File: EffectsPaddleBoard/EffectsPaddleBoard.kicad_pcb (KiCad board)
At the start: 4 copper layers, 89.6 x 66.6 mm, 90 parts, among them J1 Conn_01x03_Pin, J2 Conn_01x06_Pin, J3 Barrel_Jack, J4 Conn_01x04_Pin, J5 AudioJack2, J6 AudioJack2, SW1 SW_SPDT, SW2 SW_Push, SW3 SW_SPDT, U1 STM32F405RGTx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

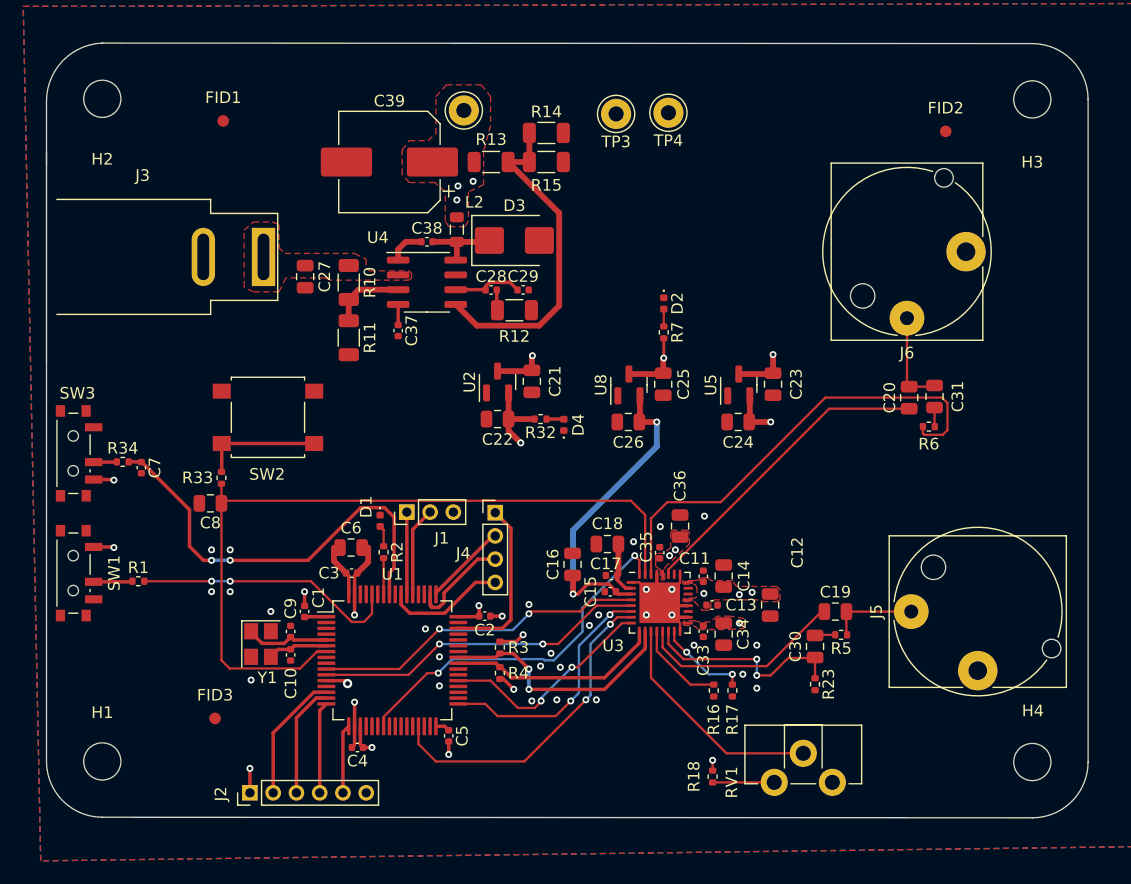
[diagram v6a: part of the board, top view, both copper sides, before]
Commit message: Eliminated all except 2 DRC errors
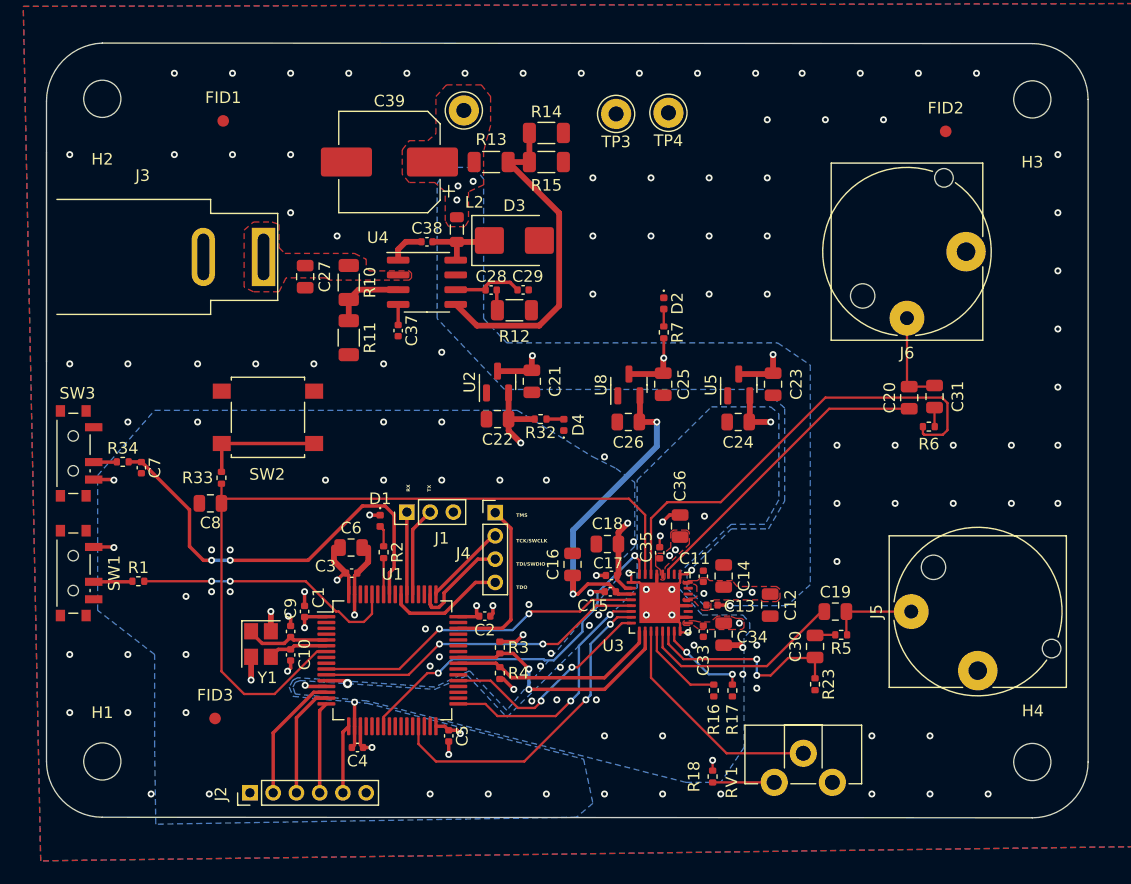
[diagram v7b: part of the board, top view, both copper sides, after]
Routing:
- net GND: track 33.2 -> 50.1 mm, vias 35 -> 136
- net +3.3V: track 34.1 -> 37.3 mm, vias 8 -> 11
- net Codec_Reset: track 67.3 -> 69.8 mm
- net +3.3VA: track 5.01 -> 6.88 mm, vias 5 -> 6
- added copper zone on B.Cu, net +3.3V
- added copper zone on B.Cu, net +3.3VA
- added copper zone on B.Cu, net +5V
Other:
- outline, holes or cut-outs redrawn
- board text added: "RX"
- board text added: "TCK/SWCLK"
- board text added: "TDI/SWDIO"
- board text added: "TDO"
- board text added: "TMS"
- board text added: "TX"

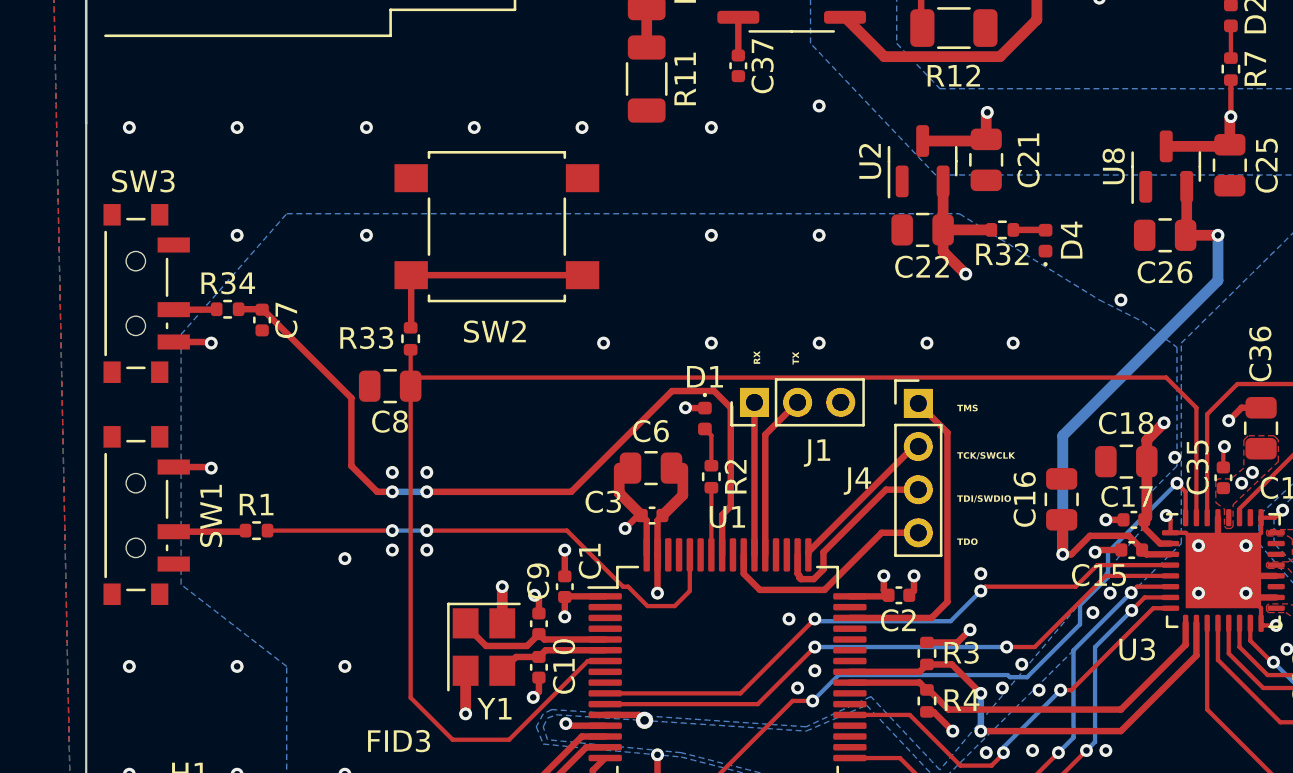
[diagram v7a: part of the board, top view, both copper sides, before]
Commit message: Added final button footprint
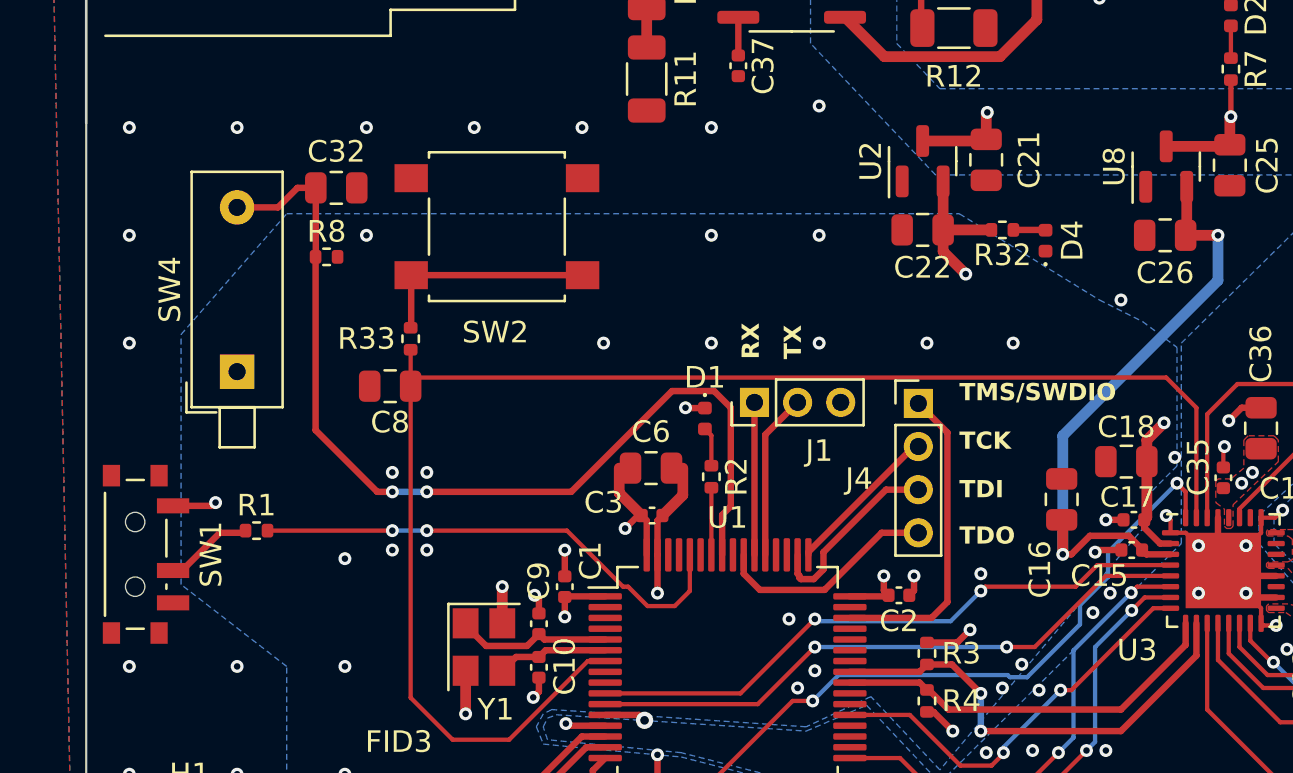
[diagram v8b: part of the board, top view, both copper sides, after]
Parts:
- removed C7: 100n, Capacitor_SMD:C_0402_1005Metric
- removed R34: 10k, Resistor_SMD:R_0402_1005Metric
- removed SW3: SW_SPDT, Button_Switch_SMD:SW_SPDT_PCM12
- added C32: 1u, Capacitor_SMD:C_0805_2012Metric, F.Cu at (132.6, 77.8)
- added R8: 220, Resistor_SMD:R_0402_1005Metric, F.Cu at (132.2, 81.0)
- added SW4: SW_Push, Button_Switch_THT:SW_DIP_SPSTx01_Piano_10.8x4.1mm_W7.62mm_P2.54mm, F.Cu at (128.0, 86.3)
- moved SW1 1.80 mm to (123.6, 94.8)
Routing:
- net On-Switch: track 37.4 -> 45.0 mm
- net Net-(SW3-B): track 2.00 -> 0.00 mm
- net +3.3V: track 37.3 -> 35.8 mm, vias 11 -> 10
- net Net-(SW1-B): track 3.35 -> 4.13 mm
- net GND: vias 136 -> 137
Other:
- board text added: "TCK"
- board text added: "TDI"
- board text added: "TMS/SWDIO"
- board text removed: "TCK/SWCLK"
- board text removed: "TDI/SWDIO"
- board text removed: "TMS"
